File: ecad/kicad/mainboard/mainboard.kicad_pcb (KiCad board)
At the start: 2 copper layers, 99.1 x 81.3 mm, 34 parts, among them IC1 74HC86, J1 SENSORS, J2 CONN_06SILK_FEMALE_PTH, J3 CONN_06SILK_FEMALE_PTH, J4 POWER, J5 SERIAL, M1 Left Motor, M2 Right Motor, U1 Arduino_Nano, U2 TB6612FNG-Module

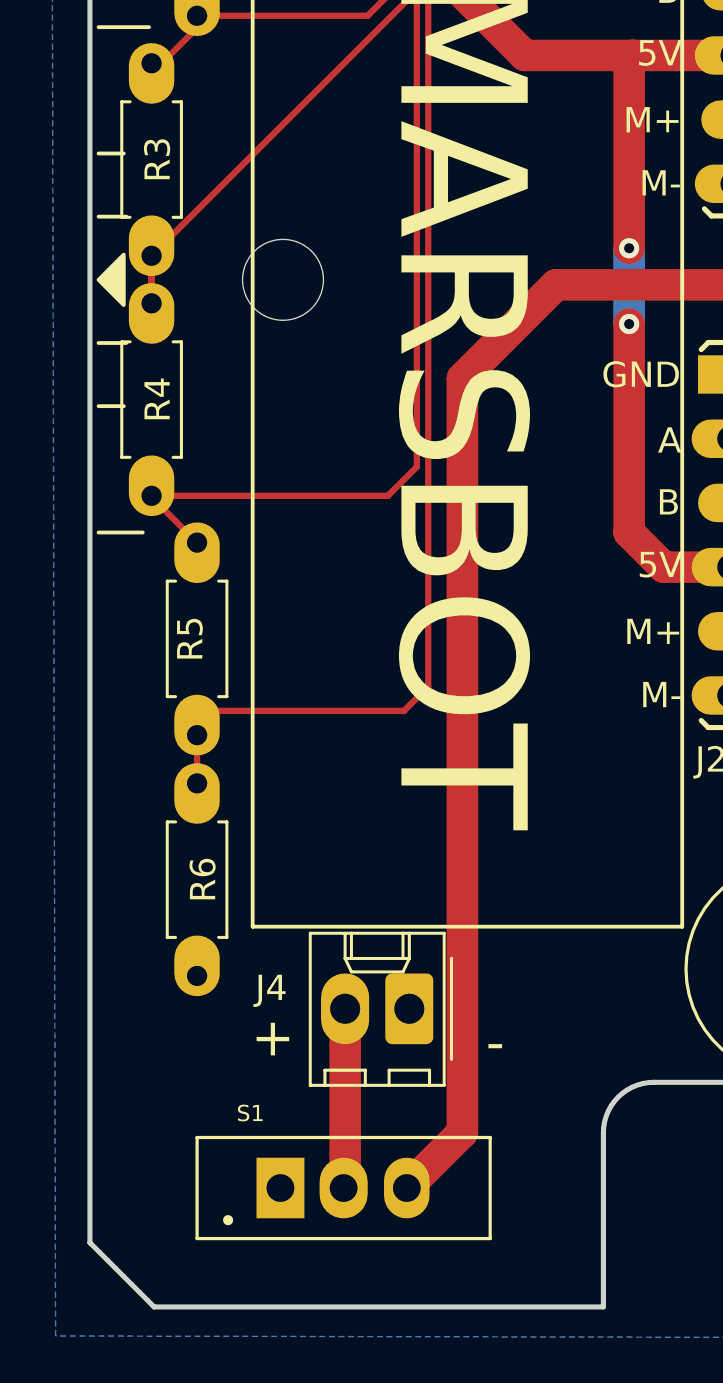
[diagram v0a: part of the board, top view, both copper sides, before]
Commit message: use new switch footprint on V1.3 board
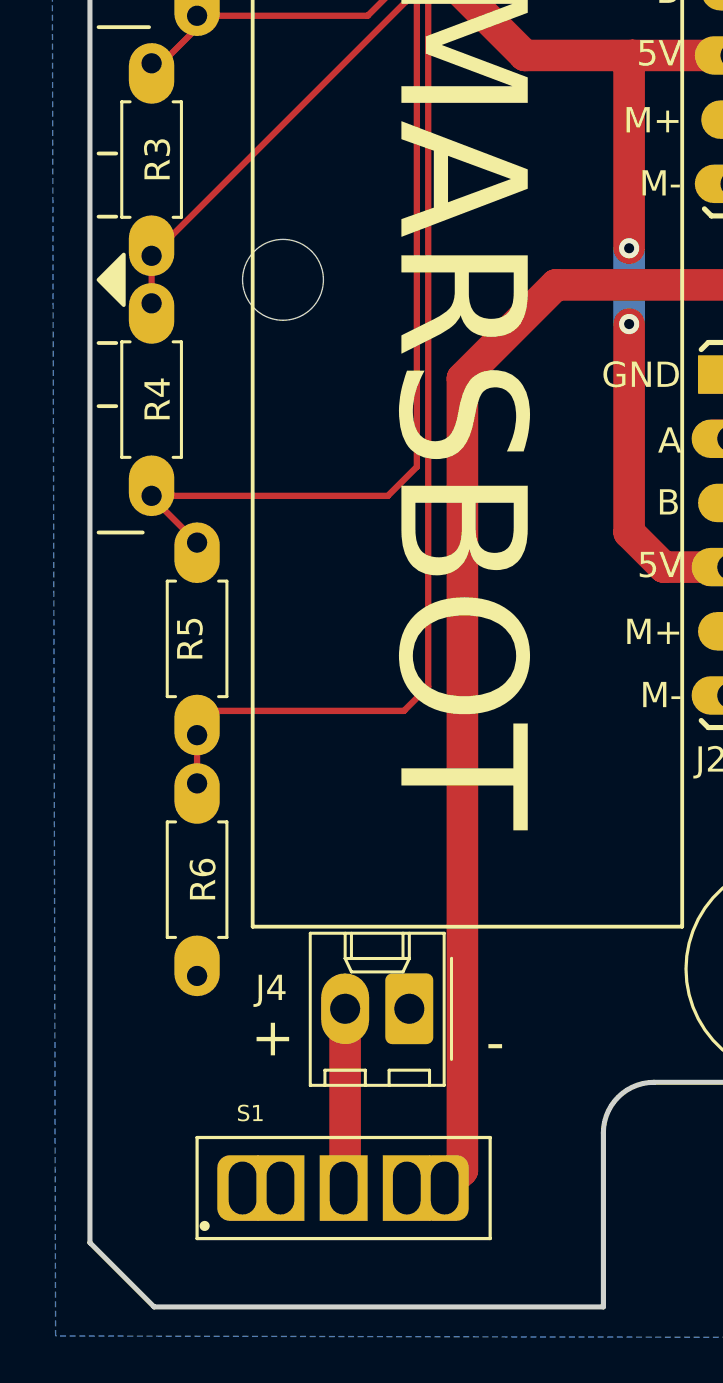
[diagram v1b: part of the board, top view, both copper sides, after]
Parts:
- S1: footprint ukmarsbot:SW_MINI_SPDT_TOGGLE_DAILYWELL_FS1S102M2QES -> ukmarsbot:SW_MINI-SPDT-RTECH-78-0564
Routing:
- net Net-(R3-Pad1): track 47.6 -> 45.9 mm
- net /SW_PWR: track 75.3 -> 74.6 mm
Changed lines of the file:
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@@
     )
   )
-  (footprint "ukmarsbot:SW_MINI_SPDT_TOGGLE_DAILYWELL_FS1S102M2QES" (layer "F.Cu")
+  (footprint "ukmarsbot:SW_MINI-SPDT-RTECH-78-0564" (layer "F.Cu")
     (at 78.2 140.944724)
-    (descr "0.1\" pitch PCB mount toggle switch")
+    (descr "0.1\" pitch PCB mount Slide switch")
     (property "Note" "Toggle or slide, 0.1\" pitch pins, EG Salecom TS-4-TE1CR-E-H-Z03")
     (property "Sheetfile" "mainboard.kicad_sch")
@@
       (effects (font (size 0.64 0.64) (thickness 0.15)))
     )
-    (fp_line (start 5.8 2) (end 5.8 -2) (layer "F.SilkS") (width 0.127))
     (fp_line (start 5.8 -2) (end -5.8 -2) (layer "F.SilkS") (width 0.127))
-    (fp_line (start -5.8 2) (end 5.8 2) (layer "F.SilkS") (width 0.127))
     (fp_line (start -5.8 -2) (end -5.8 2) (layer "F.SilkS") (width 0.127))
-    (fp_circle (center -4.572 1.27) (end -4.472 1.27) (layer "F.SilkS") (width 0.2) (fill none))
+    (fp_line (start -5.8 2) (end 5.8 2) (layer "F.SilkS") (width 0.127))
+    (fp_line (start 5.8 2) (end 5.8 -2) (layer "F.SilkS") (width 0.127))
+    (fp_circle (center -5.5 1.5) (end -5.4 1.5) (layer "F.SilkS") (width 0.2) (fill none))
     (fp_line (start 6.05 2.25) (end 6.05 -2.25) (layer "F.CrtYd") (width 0.05))
-    (fp_line (start 6.05 -2.25) (end -6.05 -2.25) (layer "F.CrtYd") (width 0.05))
     (fp_line (start -6.05 -2.25) (end -6.05 2.25) (layer "F.CrtYd") (width 0.05))
     (fp_line (start -6.05 2.25) (end 6.05 2.25) (layer "F.CrtYd") (width 0.05))
-    (fp_line (start -5.8 -2) (end -5.8 2) (layer "F.Fab") (width 0.127))
-    (fp_line (start 5.8 -2) (end -5.8 -2) (layer "F.Fab") (width 0.127))
-    (fp_line (start 5.8 2) (end 5.8 -2) (layer "F.Fab") (width 0.127))
+    (fp_line (start 6.05 -2.25) (end -6.05 -2.25) (layer "F.CrtYd") (width 0.05))
     (fp_line (start -5.8 2) (end 5.8 2) (layer "F.Fab") (width 0.127))
-    (fp_circle (center -4.572 1.27) (end -4.472 1.27) (layer "F.Fab") (width 0.2) (fill none))
-    (pad "1" thru_hole rect (at -2.5 0) (size 1.9 2.4) (drill 1.1) (layers *.Cu *.Mask)
+    (fp_line (start 5.8 2) (end 5.8 -2) (layer "F.Fab") (width 0.127))
+    (fp_line (start 5.8 -2) (end -5.8 -2) (layer "F.Fab") (width 0.127))
+    (fp_line (start -5.8 -2) (end -5.8 2) (layer "F.Fab") (width 0.127))
+    (fp_circle (center -5.5 1.5) (end -5.4 1.5) (layer "F.Fab") (width 0.2) (fill none))
+    (pad "1" thru_hole rect (at -2.5 0) (size 1.9 2.6) (drill oval 1.1 2.1) (layers *.Cu *.Mask)
       (net 43 "unconnected-(S1-Pad1)") (pinfunction "O") (pintype "passive+no_connect"))
-    (pad "2" thru_hole oval (at 0 0) (size 1.9 2.4) (drill 1.1) (layers *.Cu *.Mask)
+    (pad "1" thru_hole roundrect (at -4 0) (size 2 2.6) (drill oval 1.1 2.1) (layers *.Cu *.Mask) (roundrect_rratio 0.25)
+      (net 43 "unconnected-(S1-Pad1)") (pinfunction "O") (pintype "passive+no_connect"))
+    (pad "2" thru_hole rect (at 0 0) (size 1.9 2.6) (drill oval 1.1 2.1) (layers *.Cu *.Mask)
       (net 34 "/PWR_IN") (pinfunction "P") (pintype "passive"))
-    (pad "3" thru_hole oval (at 2.5 0) (size 1.8 2.4) (drill 1.1) (layers *.Cu *.Mask)
+    (pad "3" thru_hole roundrect (at 4 0) (size 1.9 2.6) (drill oval 1.1 2.1) (layers *.Cu *.Mask) (roundrect_rratio 0.25)
+      (net 30 "/SW_PWR") (pinfunction "S") (pintype "passive"))
+    (pad "3" thru_hole rect (at 2.5 0) (size 1.9 2.6) (drill oval 1.1 2.1) (layers *.Cu *.Mask)
       (net 30 "/SW_PWR") (pinfunction "S") (pintype "passive"))
-    (model "${KIPRJMOD}/../libraries/3D-models/buttons-switches/toggle_switch_dailywell_1AS1T2B4M2QE.step"
-      (offset (xyz 0 0 10.5))
+    (model "${KIPRJMOD}/../libraries/3D-models/buttons-switches/MINI-SPDT-SW.step"
+      (offset (xyz 0 0 0))
       (scale (xyz 1 1 1))
-      (rotate (xyz 0 0 0))
+      (rotate (xyz 90 -180 0))
     )
   )
@@
       (xy 69.5 104)
     ) (layer "F.SilkS") (width 0.15) (fill solid))
-  (gr_line (start 68.5 110) (end 69.5 110) (layer "F.SilkS") (width 0.15))
-  (gr_line (start 68.5 107.5) (end 69.6 107.5) (layer "F.SilkS") (width 0.15))
+  (gr_line (start 68.5 110) (end 69.2 110) (layer "F.SilkS") (width 0.15))
+  (gr_line (start 68.5 107.5) (end 69.2 107.5) (layer "F.SilkS") (width 0.15))
   (gr_line (start 167 102.5) (end 165 102.5) (layer "F.SilkS") (width 0.15))
   (gr_line (start 167 95) (end 164 95) (layer "F.SilkS") (width 0.15))
@@
       (xy 165 103.5)
     ) (layer "F.SilkS") (width 0.15) (fill solid))
-  (gr_line (start 68.5 102.5) (end 69.6 102.5) (layer "F.SilkS") (width 0.15))
+  (gr_line (start 68.5 102.5) (end 69.2 102.5) (layer "F.SilkS") (width 0.15))
   (gr_line (start 167 107.5) (end 165 107.5) (layer "F.SilkS") (width 0.15))
-  (gr_line (start 68.5 100) (end 69.5 100) (layer "F.SilkS") (width 0.15))
+  (gr_line (start 68.5 100) (end 69.2 100) (layer "F.SilkS") (width 0.15))
   (gr_line (start 68.5 95) (end 70.5 95) (layer "F.SilkS") (width 0.15))
   (gr_arc locked (start 139.5 68) (mid 142 65.5) (end 144.5 68) (layer "Edge.Cuts") (width 0.1))
@@
   (via (at 127.25 87.2) (size 0.8) (drill 0.4) (layers "F.Cu" "B.Cu") (net 29))
   (segment (start 130.7265 87.2) (end 127.25 87.2) (width 0.254) (layer "B.Cu") (net 29))
-  (segment (start 82.9 108.9) (end 82.9 138.744724) (width 1.25) (layer "F.Cu") (net 30))
+  (segment (start 82.9 140.244724) (end 82.2 140.944724) (width 1.25) (layer "F.Cu") (net 30))
   (segment (start 115.050499 105.199501) (end 117 103.25) (width 1.25) (layer "F.Cu") (net 30))
   (segment locked (start 86.600499 105.199501) (end 115.050499 105.199501) (width 1.25) (layer "F.Cu") (net 30))
-  (segment (start 82.9 108.9) (end 86.600499 105.199501) (width 1.25) (layer "F.Cu") (net 30))
-  (segment (start 82.9 138.744724) (end 80.7 140.944724) (width 1.25) (layer "F.Cu") (net 30))
+  (segment (start 82.9 108.9) (end 82.9 140.244724) (width 1.25) (layer "F.Cu") (net 30))
+  (segment (start 86.600499 105.199501) (end 82.9 108.9) (width 1.25) (layer "F.Cu") (net 30))
   (segment (start 117 103.25) (end 117 97.38) (width 1.25) (layer "F.Cu") (net 30))
   (segment (start 78.15 70.99) (end 80.159002 70.99) (width 0.25) (layer "F.Cu") (net 31))
@@
   (segment (start 80.199501 69.550499) (end 81.3 68.45) (width 0.25) (layer "F.Cu") (net 31))
   (segment (start 80.199501 75.13802) (end 80.198499 75.137018) (width 0.25) (layer "F.Cu") (net 31))
-  (segment (start 71 105.93) (end 70.6 105.53) (width 0.25) (layer "F.Cu") (net 32))
   (segment (start 70.6 104.05) (end 80.649002 94.000998) (width 0.25) (layer "F.Cu") (net 32))
+  (segment (start 70.6 105.93) (end 70.6 104.05) (width 0.25) (layer "F.Cu") (net 32))
   (segment (start 80.649002 94.000998) (end 80.649002 74.950998) (width 0.25) (layer "F.Cu") (net 32))
-  (segment (start 70.6 104.05) (end 70.6 105.93) (width 0.25) (layer "F.Cu") (net 32))
   (segment (start 80.65 73.85) (end 80.65 74.95) (width 0.254) (layer "F.Cu") (net 32))
   (segment (start 70.6 104.45) (end 71 104.05) (width 0.25) (layer "F.Cu") (net 32))
   (segment (start 80.649002 74.950998) (end 80.65 74.95) (width 0.25) (layer "F.Cu") (net 32))
-  (segment (start 70.6 105.53) (end 70.6 104.45) (width 0.25) (layer "F.Cu") (net 32))
   (segment (start 83.51 70.99) (end 85.77 70.99) (width 0.254) (layer "F.Cu") (net 32))
   (segment (start 80.95 73.55) (end 83.51 70.99) (width 0.254) (layer "F.Cu") (net 32))
